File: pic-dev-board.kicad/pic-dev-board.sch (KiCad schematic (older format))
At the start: 43 parts, among them J1 Conn_GP0, J13 Conn_5V_GND, J15 Barrel_Jack_Switch, J16 RUN/~PGM, J17 I2C, J18 GP1(RA1)/RB6, J19 GP2(RA2)/RB4, J2 Conn_GP4, J3 Conn_GP1, J4 Conn_GP5, J5 Conn_GP2, J6 Conn_ICSP, J7 Conn_TRISC, J8 Conn_TRISA, J9 Conn_TRISB, SW1 SW_Push, U1 PIC16F690-IP

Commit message: added +5V/GND to TRIS_* connectorS
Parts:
- J13: symbol Connector_Generic:Conn_02x15_Counter_Clockwise -> Connector_Generic:Conn_02x15_Odd_Even
- J7: footprint Connector_PinHeader_2.54mm:PinHeader_1x08_P2.54mm_Vertical -> Connector_PinHeader_2.54mm:PinHeader_1x10_P2.54mm_Vertical; symbol Connector:Conn_01x08_Male -> Connector:Conn_01x10_Male
- J8: footprint Connector_PinHeader_2.54mm:PinHeader_1x05_P2.54mm_Vertical -> Connector_PinHeader_2.54mm:PinHeader_1x07_P2.54mm_Vertical; symbol Connector:Conn_01x05_Male -> Connector:Conn_01x07_Male
- J9: footprint Connector_PinHeader_2.54mm:PinHeader_1x04_P2.54mm_Vertical -> Connector_PinHeader_2.54mm:PinHeader_1x06_P2.54mm_Vertical; symbol Connector:Conn_01x04_Male -> Connector:Conn_01x06_Male
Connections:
- net +5V: now also J13.10 (Pin_10), J13.12 (Pin_12), J13.14 (Pin_14), J13.2 (Pin_2), J13.4 (Pin_4), J13.6 (Pin_6), J13.8 (Pin_8), J7.10 (Pin_10), J8.7 (Pin_7), J9.6 (Pin_6); no longer J13.17 (Pin_17), J13.19 (Pin_19), J13.21 (Pin_21), J13.23 (Pin_23), J13.25 (Pin_25), J13.27 (Pin_27), J13.29 (Pin_29)
- net GND: now also J13.17 (Pin_17), J13.19 (Pin_19), J13.21 (Pin_21), J13.23 (Pin_23), J13.25 (Pin_25), J13.27 (Pin_27), J13.29 (Pin_29), J7.9 (Pin_9), J8.6 (Pin_6), J9.5 (Pin_5); no longer J13.10 (Pin_10), J13.12 (Pin_12), J13.14 (Pin_14), J13.2 (Pin_2), J13.4 (Pin_4), J13.6 (Pin_6), J13.8 (Pin_8)
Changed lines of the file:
@@
 $EndComp
 $Comp
-L Connector:Conn_01x05_Male J8
+L Connector:Conn_01x07_Male J8
 U 1 1 5F34B8FA
 P 1400 6850
-F 0 "J8" H 1600 6400 50  0000 R CNN
-F 1 "Conn_TRISA" H 1800 6500 50  0000 R CNN
-F 2 "Connector_PinHeader_2.54mm:PinHeader_1x05_P2.54mm_Vertical" H 1400 6850 50  0001 C CNN
+F 0 "J8" H 1600 6000 50  0000 R CNN
+F 1 "Conn_TRISA" H 1750 6100 50  0000 R CNN
+F 2 "Connector_PinHeader_2.54mm:PinHeader_1x07_P2.54mm_Vertical" H 1400 6850 50  0001 C CNN
 F 3 "~" H 1400 6850 50  0001 C CNN
 	1    1400 6850
@@
 Wire Wire Line
 	3150 4700 3150 4450
-Text Notes 1050 7200 0    50   ~ 0
+Text Notes 1050 7250 0    50   ~ 0
 GPIO/TRISA
-Text Label 1200 7050 2    50   ~ 0
+Text Label 1200 7150 2    50   ~ 0
 GP0
 $Comp
@@
 Wire Wire Line
 	2750 5300 2750 5200
-Text Label 1200 6950 2    50   ~ 0
+Text Label 1200 7050 2    50   ~ 0
 GP1
 Text Label 3250 5100 0    50   ~ 0
@@
 Wire Wire Line
 	2650 5300 2750 5300
-Text Label 1200 6850 2    50   ~ 0
+Text Label 1200 6950 2    50   ~ 0
 GP2
 Text Label 3700 4550 2    50   ~ 0
 GP2
+Text Label 1200 6850 2    50   ~ 0
+GP4
 Text Label 1200 6750 2    50   ~ 0
-GP4
-Text Label 1200 6650 2    50   ~ 0
 GP5
 Text Label 1300 850  2    50   ~ 0
@@
 GP5
 $Comp
-L Connector:Conn_01x04_Male J9
+L Connector:Conn_01x06_Male J9
 U 1 1 5F386F08
 P 2000 6950
-F 0 "J9" H 2250 6450 50  0000 R CNN
-F 1 "Conn_TRISB" H 2350 6550 50  0000 R CNN
-F 2 "Connector_PinHeader_2.54mm:PinHeader_1x04_P2.54mm_Vertical" H 2000 6950 50  0001 C CNN
+F 0 "J9" H 2250 6000 50  0000 R CNN
+F 1 "Conn_TRISB" H 2350 6100 50  0000 R CNN
+F 2 "Connector_PinHeader_2.54mm:PinHeader_1x06_P2.54mm_Vertical" H 2000 6950 50  0001 C CNN
 F 3 "~" H 2000 6950 50  0001 C CNN
 	1    2000 6950
 	-1   0    0    1
 $EndComp
-Text Notes 1700 7200 0    50   ~ 0
+Text Notes 1750 7250 0    50   ~ 0
 TRISB
-Text Label 1800 7050 2    50   ~ 0
+Text Label 1800 7150 2    50   ~ 0
 RB4
 Text Label 3700 5050 2    50   ~ 0
@@
 Text Label 3700 5350 2    50   ~ 0
 RB7
+Text Label 1800 7050 2    50   ~ 0
+RB5
 Text Label 1800 6950 2    50   ~ 0
-RB5
+RB6
 Text Label 1800 6850 2    50   ~ 0
-RB6
-Text Label 1800 6750 2    50   ~ 0
 RB7
 $Comp
-L Connector:Conn_01x08_Male J7
+L Connector:Conn_01x10_Male J7
 U 1 1 5F38A390
 P 2600 6750
-F 0 "J7" H 2750 6050 50  0000 C CNN
-F 1 "Conn_TRISC" H 2750 6200 50  0000 C CNN
-F 2 "Connector_PinHeader_2.54mm:PinHeader_1x08_P2.54mm_Vertical" H 2600 6750 50  0001 C CNN
+F 0 "J7" H 2750 6000 50  0000 C CNN
+F 1 "Conn_TRISC" H 2750 6100 50  0000 C CNN
+F 2 "Connector_PinHeader_2.54mm:PinHeader_1x10_P2.54mm_Vertical" H 2600 6750 50  0001 C CNN
 F 3 "~" H 2600 6750 50  0001 C CNN
 	1    2600 6750
 	-1   0    0    1
 $EndComp
-Text Notes 2350 7200 0    50   ~ 0
+Text Notes 2350 7250 0    50   ~ 0
 TRISC
+Text Label 2400 7150 2    50   ~ 0
+RC0
 Text Label 2400 7050 2    50   ~ 0
-RC0
+RC1
 Text Label 2400 6950 2    50   ~ 0
-RC1
+RC2
 Text Label 2400 6850 2    50   ~ 0
-RC2
+RC3
 Text Label 2400 6750 2    50   ~ 0
-RC3
+RC4
 Text Label 2400 6650 2    50   ~ 0
-RC4
+RC5
 Text Label 2400 6550 2    50   ~ 0
-RC5
+RC6
 Text Label 2400 6450 2    50   ~ 0
-RC6
-Text Label 2400 6350 2    50   ~ 0
 RC7
 Text Label 6700 4350 0    50   ~ 0
@@
 2x SN74HC595 shift register
 $Comp
-L Connector_Generic:Conn_02x15_Counter_Clockwise J13
+L Connector_Generic:Conn_02x15_Odd_Even J13
 U 1 1 5F3C7703
 P 5950 6850
@@
 Wire Wire Line
 	6550 7050 6450 7050
+$Comp
+L power:GND #PWR0105
+U 1 1 5F3EAAD0
+P 1000 6350
+F 0 "#PWR0105" H 1000 6100 50  0001 C CNN
+F 1 "GND" H 950 6200 50  0000 C CNN
+F 2 "" H 1000 6350 50  0001 C CNN
+F 3 "" H 1000 6350 50  0001 C CNN
+	1    1000 6350
+	1    0    0    -1
+$EndComp
+$Comp
+L power:+5V #PWR0106
+U 1 1 5F3EB6C7
+P 1000 6250
+F 0 "#PWR0106" H 1000 6100 50  0001 C CNN
+F 1 "+5V" H 950 6400 50  0000 C CNN
+F 2 "" H 1000 6250 50  0001 C CNN
+F 3 "" H 1000 6250 50  0001 C CNN
+	1    1000 6250
+	1    0    0    -1
+$EndComp
+Wire Wire Line
+	1000 6350 1100 6350
+Wire Wire Line
+	1100 6350 1100 6650
+Wire Wire Line
+	1100 6650 1200 6650
+Wire Wire Line
+	1100 6350 1700 6350
+Connection ~ 1100 6350
+Wire Wire Line
+	1000 6250 1200 6250
+Wire Wire Line
+	1200 6250 1200 6550
+Connection ~ 1200 6250
+Wire Wire Line
+	1200 6250 1800 6250
+Wire Wire Line
+	1800 6750 1700 6750
+Wire Wire Line
+	1700 6750 1700 6350
+Connection ~ 1700 6350
+Wire Wire Line
+	1700 6350 2400 6350
+Wire Wire Line
+	1800 6650 1800 6250
+Connection ~ 1800 6250
+Wire Wire Line
+	1800 6250 2400 6250
 $EndSCHEMATC

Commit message: fixed footprint for poti
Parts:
- RV1: footprint Potentiometer_THT:Potentiometer_Bourns_3386X_Horizontal -> user:TRIM_3362P-1-103
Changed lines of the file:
@@
 F 0 "RV1" H 8331 5304 50  0000 R CNN
 F 1 "10K" H 8331 5395 50  0000 R CNN
-F 2 "Potentiometer_THT:Potentiometer_Bourns_3386X_Horizontal" H 8400 5350 50  0001 C CNN
+F 2 "user:TRIM_3362P-1-103" H 8400 5350 50  0001 C CNN
 F 3 "~" H 8400 5350 50  0001 C CNN
 	1    8400 5350

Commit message: updated footprint for +5V/GND connector
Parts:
- J13: footprint Connector_PinHeader_2.54mm:PinHeader_2x15_P2.54mm_Vertical -> user:PinHeader_2x15_P2.54mm_Vertical_Slim
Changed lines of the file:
@@
 F 0 "J13" V 6450 7000 50  0000 R CNN
 F 1 "Conn_5V_GND" V 6350 7150 50  0000 R CNN
-F 2 "Connector_PinHeader_2.54mm:PinHeader_2x15_P2.54mm_Vertical" H 5950 6850 50  0001 C CNN
+F 2 "user:PinHeader_2x15_P2.54mm_Vertical_Slim" H 5950 6850 50  0001 C CNN
 F 3 "~" H 5950 6850 50  0001 C CNN
 	1    5950 6850

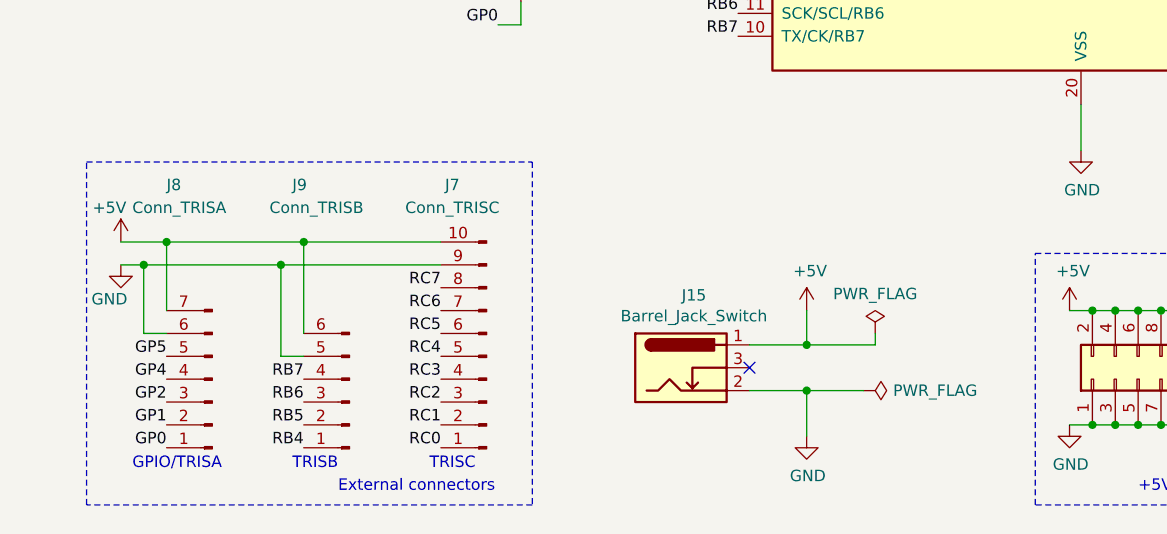
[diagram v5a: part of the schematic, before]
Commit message: added second GP/TRISA connector
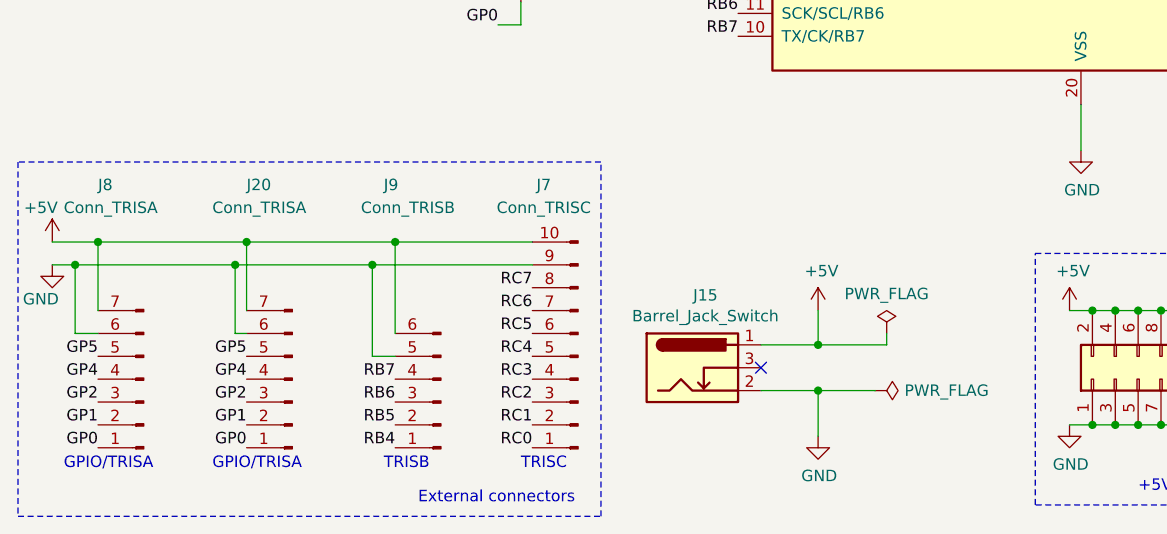
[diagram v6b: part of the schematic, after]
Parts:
- added J20: Conn_TRISA, Connector_PinHeader_2.54mm:PinHeader_1x07_P2.54mm_Vertical, symbol Connector:Conn_01x07_Male
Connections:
- net +5V: now also J20.7 (Pin_7)
- net GND: now also J20.6 (Pin_6)
- net GP0: now also J20.1 (Pin_1)
- net GP1: now also J20.2 (Pin_2)
- net GP2: now also J20.3 (Pin_3)
- net GP4: now also J20.4 (Pin_4)
- net GP5: now also J20.5 (Pin_5)
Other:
- moved on the sheet: J15, J7, J8, J9

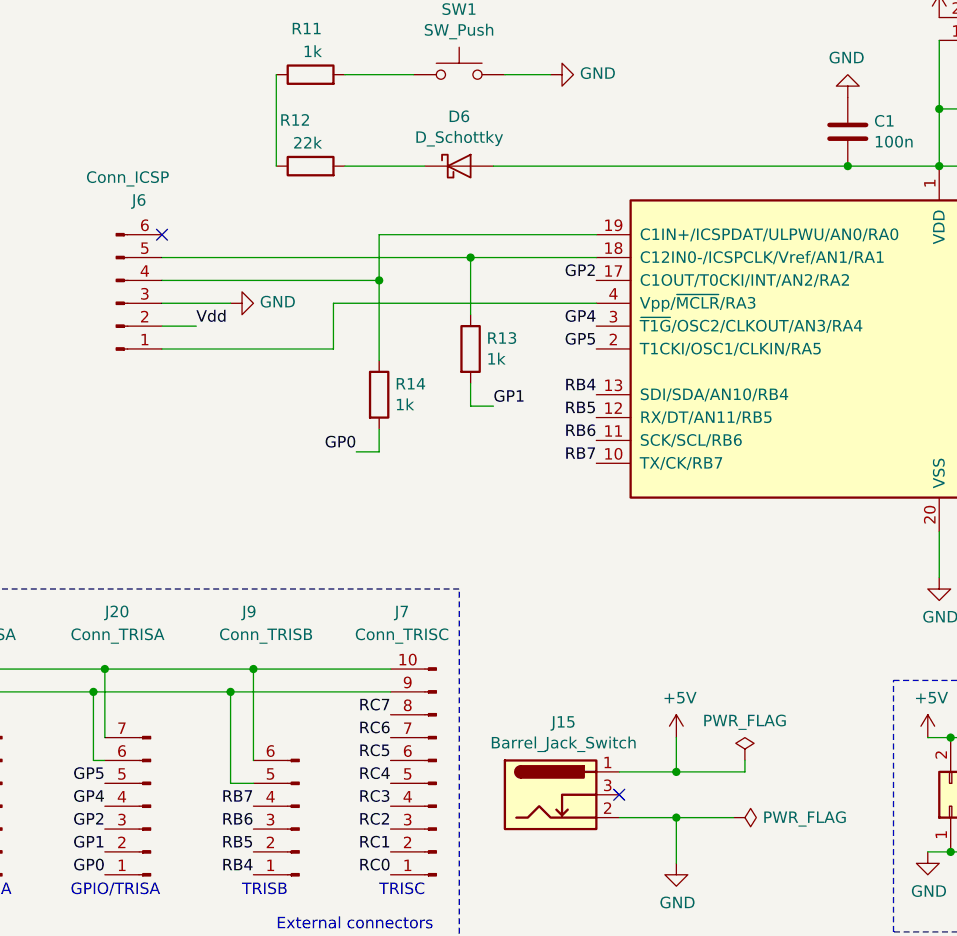
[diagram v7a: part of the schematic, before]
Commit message: bugfixes: no Vdd connection to barrel-jack, missing connection Vpp to R11/R12
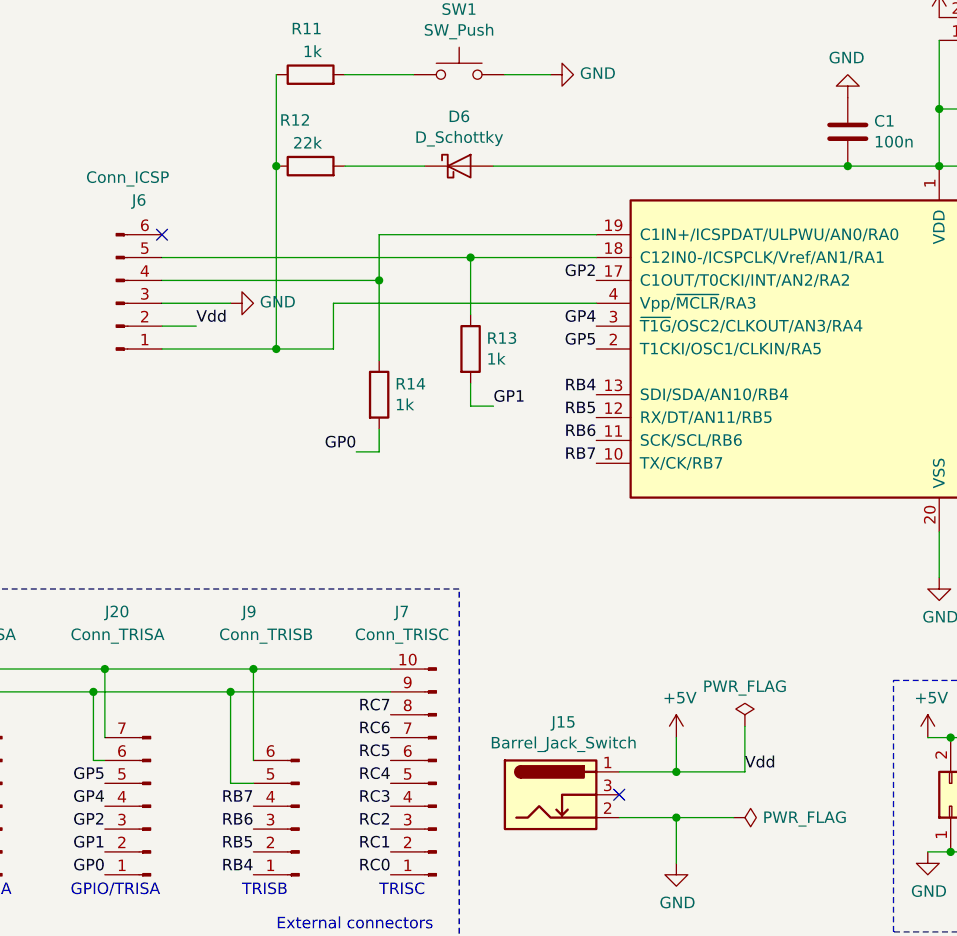
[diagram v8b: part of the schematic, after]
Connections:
- net Vdd is gone; now on net +5V: C1.2, D6.2 (A), J16.1 (Pin_1), J6.2 (Pin_2), U1.1 (VDD)
- net at J6.1 (Pin_1), U1.4 (Vpp/~MCLR~/RA3): now also R11.1, R12.1
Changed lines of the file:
@@
 Sheet 1 2
 Title "PIC Development Board"
-Date "2020-08-21"
-Rev "1"
+Date "2020-08-24"
+Rev "2"
 Comp "Bernhard Bablok"
 Comment1 "https://github.com/bablokb/pcb-pic-devboard"
@@
 	2550 4650 2550 4850
 Wire Wire Line
-	1800 4850 2550 4850
+	1800 4850 2300 4850
 Wire Wire Line
 	2550 4650 3700 4650
@@
 L power:PWR_FLAG #FLG0102
 U 1 1 5F3F0E86
-P 4350 6650
-F 0 "#FLG0102" H 4350 6725 50  0001 C CNN
-F 1 "PWR_FLAG" H 4350 6823 50  0000 C CNN
-F 2 "" H 4350 6650 50  0001 C CNN
-F 3 "~" H 4350 6650 50  0001 C CNN
-	1    4350 6650
+P 4350 6500
+F 0 "#FLG0102" H 4350 6575 50  0001 C CNN
+F 1 "PWR_FLAG" H 4350 6673 50  0000 C CNN
+F 2 "" H 4350 6500 50  0001 C CNN
+F 3 "~" H 4350 6500 50  0001 C CNN
+	1    4350 6500
 	1    0    0    -1
 $EndComp
@@
 Wire Wire Line
 	4050 6700 4350 6700
-Wire Wire Line
-	4350 6700 4350 6650
 Connection ~ 4050 6700
 Wire Wire Line
@@
 Wire Notes Line
 	3100 7450 3100 5900
+Text Label 4350 6700 0    50   ~ 0
+Vdd
+Wire Wire Line
+	4350 6500 4350 6700
+Wire Wire Line
+	2300 4050 2300 4850
+Connection ~ 2300 4050
+Connection ~ 2300 4850
+Wire Wire Line
+	2300 4850 2550 4850
 $EndSCHEMATC
